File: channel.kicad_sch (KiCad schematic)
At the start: 8 parts, among them Q5 MMBT5551, Q6 SiS402DN, Q7 SiS402DN, Q8 MMBT5401

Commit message: order files
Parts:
- renumbered C12 to C13, C13 to C14, Q8 to Q6, Q6 to Q7, Q7 to Q8, R13 to R15
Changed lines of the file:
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@@
   (symbol (lib_id "power:GND") (at 76.2 67.31 0)
     (in_bom yes) (on_board yes)
-    (property "Reference" "#PWR036" (id 0) (at 76.2 73.66 0)
+    (property "Reference" "#PWR035" (id 0) (at 76.2 73.66 0)
       (effects (font (size 1.27 1.27)) hide)
     )
@@
   (symbol (lib_id "power:GND") (at 40.64 69.85 0)
     (in_bom yes) (on_board yes)
-    (property "Reference" "#PWR037" (id 0) (at 40.64 76.2 0)
+    (property "Reference" "#PWR034" (id 0) (at 40.64 76.2 0)
       (effects (font (size 1.27 1.27)) hide)
     )
@@
   (symbol (lib_id "power:GND") (at 105.41 57.15 0)
     (in_bom yes) (on_board yes)
-    (property "Reference" "#PWR035" (id 0) (at 105.41 63.5 0)
+    (property "Reference" "#PWR036" (id 0) (at 105.41 63.5 0)
       (effects (font (size 1.27 1.27)) hide)
     )
@@
   (symbol (lib_id "Device:Q_PNP_BEC") (at 73.66 62.23 0) (mirror x)
     (in_bom yes) (on_board yes)
-    (property "Reference" "Q8" (id 0) (at 78.5114 61.0616 0)
+    (property "Reference" "Q6" (id 0) (at 78.5114 61.0616 0)
       (effects (font (size 1.27 1.27)) (justify left))
     )
@@
   (symbol (lib_id "Device:R") (at 87.63 49.53 90)
     (in_bom yes) (on_board yes)
-    (property "Reference" "R13" (id 0) (at 87.63 44.2722 90))
+    (property "Reference" "R15" (id 0) (at 87.63 44.2722 90))
     (property "Value" "100" (id 1) (at 87.63 46.5836 90))
     (property "Footprint" "Resistor_SMD:R_0402_1005Metric_Pad0.72x0.64mm_HandSolder" (id 2) (at 87.63 51.308 90)
@@
   (symbol (lib_id "Device:C") (at 105.41 53.34 0)
     (in_bom yes) (on_board yes)
-    (property "Reference" "C13" (id 0) (at 102.489 52.1716 0)
+    (property "Reference" "C14" (id 0) (at 102.489 52.1716 0)
       (effects (font (size 1.27 1.27)) (justify right))
     )
@@
   (symbol (lib_id "Device:C") (at 29.21 33.02 0)
     (in_bom yes) (on_board yes)
-    (property "Reference" "C12" (id 0) (at 32.131 31.8516 0)
+    (property "Reference" "C13" (id 0) (at 32.131 31.8516 0)
       (effects (font (size 1.27 1.27)) (justify left))
     )
@@
   (symbol (lib_id "power:GND") (at 29.21 36.83 0)
     (in_bom yes) (on_board yes)
-    (property "Reference" "#PWR032" (id 0) (at 29.21 43.18 0)
+    (property "Reference" "#PWR033" (id 0) (at 29.21 43.18 0)
       (effects (font (size 1.27 1.27)) hide)
     )
@@
   (symbol (lib_id "power:GND") (at 132.08 54.61 0)
     (in_bom yes) (on_board yes)
-    (property "Reference" "#PWR033" (id 0) (at 132.08 60.96 0)
+    (property "Reference" "#PWR037" (id 0) (at 132.08 60.96 0)
       (effects (font (size 1.27 1.27)) hide)
     )
@@
   (symbol (lib_id "mark:SiS402DN") (at 129.54 49.53 0)
     (in_bom yes) (on_board yes)
-    (property "Reference" "Q6" (id 0) (at 134.7216 48.3616 0)
+    (property "Reference" "Q7" (id 0) (at 134.7216 48.3616 0)
       (effects (font (size 1.27 1.27)) (justify left))
     )
@@
   (symbol (lib_id "mark:SiS402DN") (at 158.75 49.53 0)
     (in_bom yes) (on_board yes)
-    (property "Reference" "Q7" (id 0) (at 163.9316 48.3616 0)
+    (property "Reference" "Q8" (id 0) (at 163.9316 48.3616 0)
       (effects (font (size 1.27 1.27)) (justify left))
     )
@@
   (symbol (lib_id "power:GND") (at 161.29 54.61 0)
     (in_bom yes) (on_board yes)
-    (property "Reference" "#PWR034" (id 0) (at 161.29 60.96 0)
-      (effects (font (size 1.27 1.27)) hide)
-    )
+    (property "Reference" "#PWR038" (id 0) (at 161.29 60.96 0)
+      (effects (font (size 1.27 1.27)) hide)
+    )

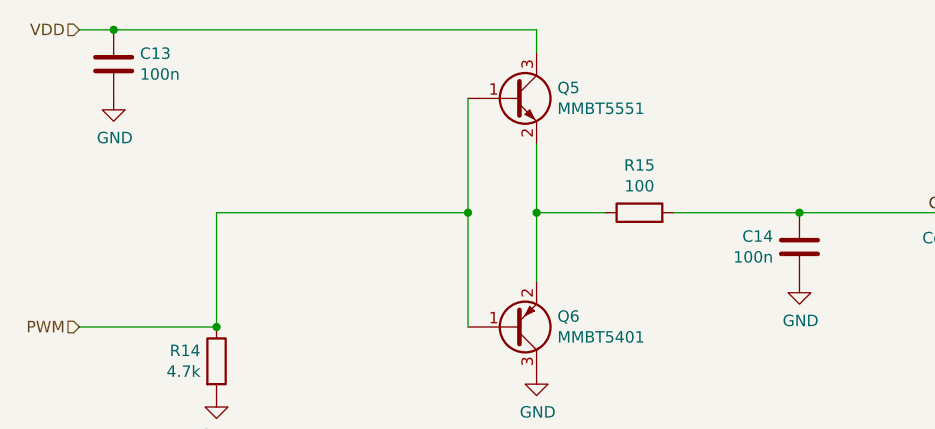
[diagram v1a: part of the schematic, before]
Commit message: fix rotary pinout, add 5v0 to header in extra-col, regen fab+doc
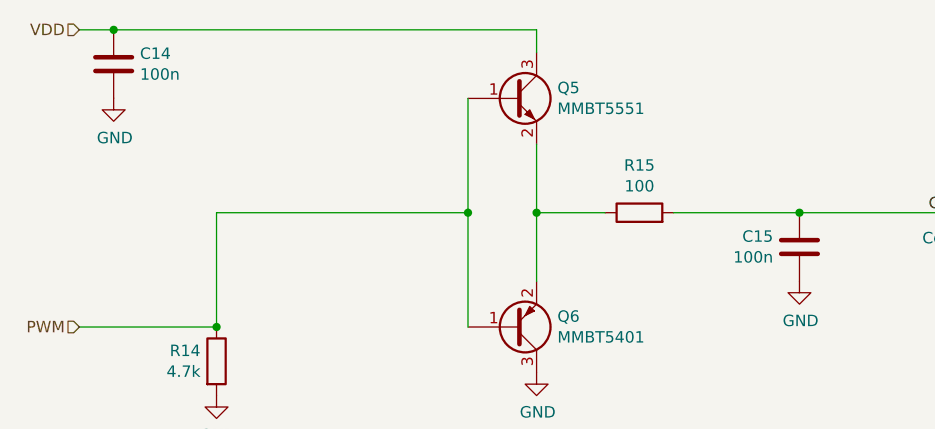
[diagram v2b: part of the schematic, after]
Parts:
- renumbered C13 to C14, C14 to C15
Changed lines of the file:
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@@
   (symbol (lib_id "power:GND") (at 76.2 67.31 0)
     (in_bom yes) (on_board yes)
-    (property "Reference" "#PWR035" (id 0) (at 76.2 73.66 0)
+    (property "Reference" "#PWR038" (id 0) (at 76.2 73.66 0)
       (effects (font (size 1.27 1.27)) hide)
     )
@@
   (symbol (lib_id "power:GND") (at 40.64 69.85 0)
     (in_bom yes) (on_board yes)
-    (property "Reference" "#PWR034" (id 0) (at 40.64 76.2 0)
+    (property "Reference" "#PWR037" (id 0) (at 40.64 76.2 0)
       (effects (font (size 1.27 1.27)) hide)
     )
@@
   (symbol (lib_id "power:GND") (at 105.41 57.15 0)
     (in_bom yes) (on_board yes)
-    (property "Reference" "#PWR036" (id 0) (at 105.41 63.5 0)
+    (property "Reference" "#PWR039" (id 0) (at 105.41 63.5 0)
       (effects (font (size 1.27 1.27)) hide)
     )
@@
   (symbol (lib_id "Device:C") (at 105.41 53.34 0)
     (in_bom yes) (on_board yes)
-    (property "Reference" "C14" (id 0) (at 102.489 52.1716 0)
+    (property "Reference" "C15" (id 0) (at 102.489 52.1716 0)
       (effects (font (size 1.27 1.27)) (justify right))
     )
@@
   (symbol (lib_id "Device:C") (at 29.21 33.02 0)
     (in_bom yes) (on_board yes)
-    (property "Reference" "C13" (id 0) (at 32.131 31.8516 0)
+    (property "Reference" "C14" (id 0) (at 32.131 31.8516 0)
       (effects (font (size 1.27 1.27)) (justify left))
     )
@@
   (symbol (lib_id "power:GND") (at 29.21 36.83 0)
     (in_bom yes) (on_board yes)
-    (property "Reference" "#PWR033" (id 0) (at 29.21 43.18 0)
+    (property "Reference" "#PWR036" (id 0) (at 29.21 43.18 0)
       (effects (font (size 1.27 1.27)) hide)
     )
@@
   (symbol (lib_id "power:GND") (at 132.08 54.61 0)
     (in_bom yes) (on_board yes)
-    (property "Reference" "#PWR037" (id 0) (at 132.08 60.96 0)
+    (property "Reference" "#PWR040" (id 0) (at 132.08 60.96 0)
       (effects (font (size 1.27 1.27)) hide)
     )
@@
   (symbol (lib_id "power:GND") (at 161.29 54.61 0)
     (in_bom yes) (on_board yes)
-    (property "Reference" "#PWR038" (id 0) (at 161.29 60.96 0)
-      (effects (font (size 1.27 1.27)) hide)
-    )
+    (property "Reference" "#PWR041" (id 0) (at 161.29 60.96 0)
+      (effects (font (size 1.27 1.27)) hide)
+    )

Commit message: improvements, notes for future TODO stuff
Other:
- note added: "D.N.P."
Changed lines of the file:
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@@
+    (effects (font (size 1.27 1.27)) (justify left bottom))
+  )
+  (text "D.N.P." (at 106.045 57.15 0)
     (effects (font (size 1.27 1.27)) (justify left bottom))
   )
